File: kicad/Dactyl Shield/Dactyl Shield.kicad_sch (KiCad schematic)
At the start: 10 parts

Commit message: feat: unchecked in changes, likely to LED
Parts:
- TP101, TP102, TP103, TP104: Config (none) -> DNF; Role (none) -> Split

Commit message: doc(sck): better notes on split wire use
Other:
- note added: "The keyboard uses left and right mirrored PCB halves of mostly the same schematic. The schematic differences (below) are for use of the hardware TX/RX for the two wire split. See the shared sub sheet for other details and descriptions."
- note removed: "The keyboard uses left and right mirrored PCB halves of mostly the same schematic. The schematic differences are to use the hardware TX/RX for two wire split. See the shared sub sheet for details and descriptions."
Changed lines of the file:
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@@
 	(title_block
 		(title "Hillside Dactyl Shield")
-		(date "2024-06-04")
+		(date "2025-01-14")
 		(rev "0.1.0-alpha.2")
 		(comment 1 "  Headers: MCU, key matrix and display")
@@
 	(polyline
 		(pts
-			(xy 36.83 171.45) (xy 36.83 203.2)
+			(xy 36.83 172.085) (xy 36.83 203.835)
 		)
 		(stroke
@@
 	(polyline
 		(pts
-			(xy 90.17 57.15) (xy 158.75 57.15)
+			(xy 102.87 50.165) (xy 171.45 50.165)
 		)
 		(stroke
@@
 	(polyline
 		(pts
-			(xy 158.75 67.31) (xy 90.17 67.31)
-		)
-		(stroke
-			(width 0)
-			(type default)
-		)
-	)
-	(polyline
-		(pts
-			(xy 90.17 57.15) (xy 90.17 67.31)
+			(xy 171.45 60.325) (xy 102.87 60.325)
+		)
+		(stroke
+			(width 0)
+			(type default)
+		)
+	)
+	(polyline
+		(pts
+			(xy 102.87 50.165) (xy 102.87 60.325)
 		)
 		(stroke
@@
 	(polyline
 		(pts
-			(xy 158.75 57.15) (xy 158.75 67.31)
+			(xy 171.45 50.165) (xy 171.45 60.325)
 		)
 		(stroke
@@
 	(polyline
 		(pts
-			(xy 158.75 171.45) (xy 36.83 171.45)
-		)
-		(stroke
-			(width 0)
-			(type dash)
-		)
-	)
-	(text_box "Hack to avoid isolated fill warnings\non the paneling side rails."
+			(xy 158.75 172.085) (xy 36.83 172.085)
+		)
+		(stroke
+			(width 0)
+			(type dash)
+		)
+	)
+	(text_box "Hack to avoid warnins about\nisolated fills on the panel side rails."
 		(exclude_from_sim no)
 		(at 107.95 181.61 0)
-		(size 36.83 6.35)
+		(size 38.735 6.35)
 		(stroke
 			(width -0.0001)
@@
 		)
 	)
-	(text_box "USB-C cable use:\n- We aren't sending USB protocal over the split USB-C cable.\n- Our split USB resistors ask for no power, but we accept 5v power in case some accidental computer host isn't doing what it should."
-		(exclude_from_sim no)
-		(at 162.56 141.605 0)
-		(size 48.26 17.78)
+	(text_box "Split USB-C cable use:\n\n- We don't send USB protocal over the split USB-C cable.\n- Yet we follow the protocal in having our split USB resistors ask for no power, and we accept 5v power in case some accidental computer host isn't doing what it should."
+		(exclude_from_sim no)
+		(at 43.815 139.065 0)
+		(size 63.5 13.97)
 		(stroke
 			(width 0)
@@
 		)
 	)
-	(text_box "Caveat:\nI'm not an electrical engineer. This is my best cut at the right approach after much reading plus creating a few boards that seem to work fine. I had EE classes within my CS degrees, but this is outside of that."
-		(exclude_from_sim no)
-		(at 194.945 45.72 0)
+	(text_box "Caveat:\nI'm not an electrical engineer. This is my best cut at the right approach after much reading plus creating a few boards that seem to work fine. I had EE classes in my CS degrees, but this is outside of that."
+		(exclude_from_sim no)
+		(at 194.945 48.895 0)
 		(size 61.595 24.13)
 		(stroke
@@
 		)
 	)
-	(text_box "The wired split can be:\n\n- One wire, though mainly right to left:\n  D+:   Left RX <-> Right TX\n\n- Two wire: \n  D+:   Left RX <-- Right TX \n  D-:   Left TX --> Right RX"
-		(exclude_from_sim no)
-		(at 111.76 139.7 0)
-		(size 45.72 20.955)
+	(text_box "With a wireless split: The UART RX and TX pins can be used for other things.\nSuch as a fifth row or the additional signal line to the Vic connector.\nThough they are wired differently on each board half.\n\nWith a one-wire split: The left RX and right TX pins carry the split, \nand the other can be used for something else.\n\nWith a two-wire split: Both UART RX and TX are used for the split."
+		(exclude_from_sim no)
+		(at 162.56 139.065 0)
+		(size 78.74 18.415)
 		(stroke
 			(width 0)
@@
 		)
 	)
+	(text_box "The wired split can be:\n\n- One wire, though mainly right to left:\n  D+:   Left RX <-> Right TX\n\n- Two wire: \n  D+:   Left RX <-- Right TX \n  D-:   Left TX --> Right RX\n\nBased on firmware needs."
+		(exclude_from_sim no)
+		(at 111.76 139.065 0)
+		(size 45.72 21.59)
+		(stroke
+			(width 0)
+			(type dash)
+		)
+		(fill
+			(type none)
+		)
+		(effects
+			(font
+				(size 1.27 1.27)
+			)
+			(justify left top)
+		)
+	)
 	(text_box "Split\nUSB-C\ncable"
 		(exclude_from_sim no)
@@
 	(text "${TITLE}"
 		(exclude_from_sim no)
-		(at 91.44 64.77 0)
+		(at 104.14 57.785 0)
 		(effects
 			(font
@@
 		)
 	)
-	(text "The keyboard uses left and right mirrored  \nPCB halves of mostly the same schematic.\n\nThe schematic differences are to use the hardware TX/RX\nfor two wire split.\n\nSee the shared sub sheet for details and descriptions."
-		(exclude_from_sim no)
-		(at 90.678 96.266 0)
+	(text "The keyboard uses left and right mirrored  \nPCB halves of mostly the same schematic.\n\nThe schematic differences (below) are for use of the \nhardware TX/RX for the two wire split.\n\nSee the shared sub sheet for other details and descriptions."
+		(exclude_from_sim no)
+		(at 90.678 95.631 0)
 		(effects
 			(font
@@
 	(label "rail_LL"
 		(at 102.87 198.12 0)
-		(fields_autoplaced yes)
 		(effects
 			(font
@@
 	(label "rail_UL"
 		(at 102.87 191.77 0)
-		(fields_autoplaced yes)
 		(effects
 			(font
@@
 	(label "rail_UR"
 		(at 132.08 191.77 0)
-		(fields_autoplaced yes)
 		(effects
 			(font
@@
 	(label "rail_LR"
 		(at 132.08 198.12 0)
-		(fields_autoplaced yes)
-		(effects
-			(font
+		(effects
+			(font

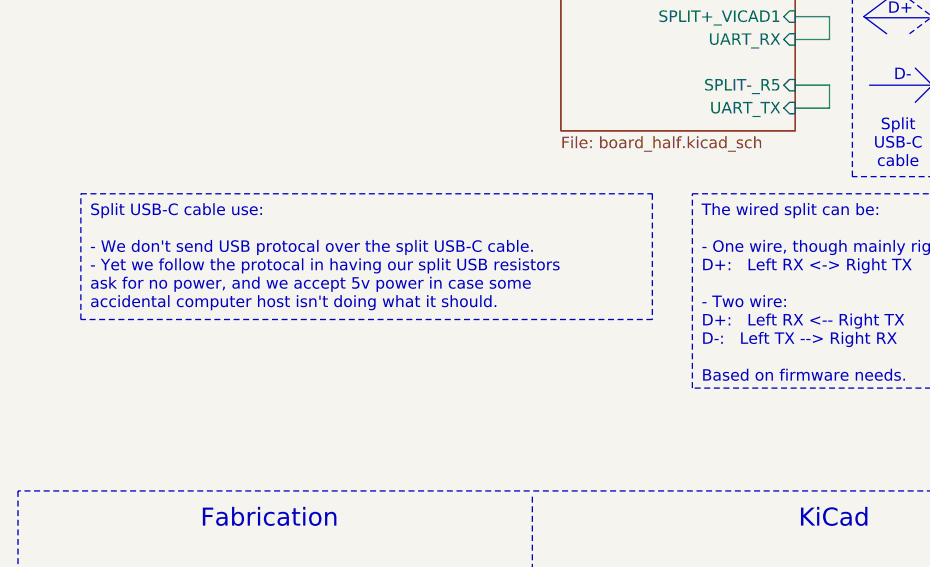
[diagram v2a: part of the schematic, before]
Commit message: refactor: cleanup schematic; external -> foot
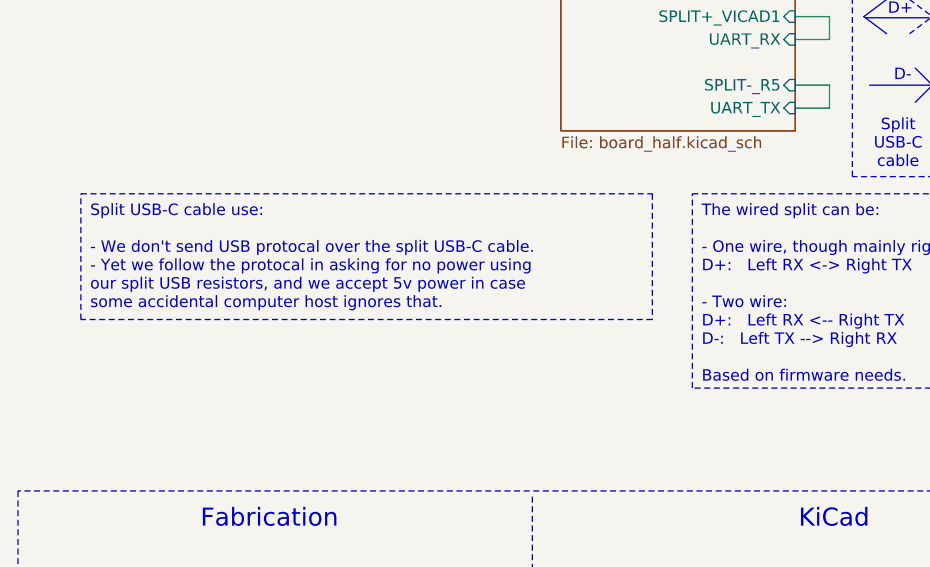
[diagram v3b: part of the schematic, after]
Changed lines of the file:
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@@
 		)
 	)
-	(text_box "Split USB-C cable use:\n\n- We don't send USB protocal over the split USB-C cable.\n- Yet we follow the protocal in having our split USB resistors ask for no power, and we accept 5v power in case some accidental computer host isn't doing what it should."
+	(text_box "Split USB-C cable use:\n\n- We don't send USB protocal over the split USB-C cable.\n- Yet we follow the protocal in asking for no power using our split USB resistors, and we accept 5v power in case some accidental computer host ignores that."
 		(exclude_from_sim no)
 		(at 43.815 139.065 0)

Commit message: feat: use open solder jumpers to LEDs
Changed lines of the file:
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@@
 (kicad_sch
-	(version 20231120)
+	(version 20250114)
 	(generator "eeschema")
-	(generator_version "8.0")
+	(generator_version "9.0")
 	(paper "USLetter")
 	(title_block
@@
 		(comment 4 "Shield for Dactyl split keyboards ")
 	)
+	(text "D-"
+		(exclude_from_sim no)
+		(at 135.128 125.984 0)
+		(effects
+			(font
+				(size 1.27 1.27)
+			)
+		)
+	)
+	(text "5v"
+		(exclude_from_sim no)
+		(at 133.985 111.125 0)
+		(effects
+			(font
+				(size 1.27 1.27)
+			)
+		)
+	)
+	(text "KiCad"
+		(exclude_from_sim no)
+		(at 127.508 175.26 0)
+		(effects
+			(font
+				(size 2 2)
+			)
+		)
+	)
+	(text "Fabrication"
+		(exclude_from_sim no)
+		(at 64.77 175.26 0)
+		(effects
+			(font
+				(size 2 2)
+			)
+		)
+	)
+	(text "${TITLE}"
+		(exclude_from_sim no)
+		(at 104.14 57.785 0)
+		(effects
+			(font
+				(size 4 4)
+			)
+			(justify left bottom)
+		)
+	)
+	(text "D+"
+		(exclude_from_sim no)
+		(at 134.874 118.618 0)
+		(effects
+			(font
+				(size 1.27 1.27)
+			)
+		)
+	)
+	(text "GND"
+		(exclude_from_sim no)
+		(at 133.985 114.935 0)
+		(effects
+			(font
+				(size 1.27 1.27)
+			)
+		)
+	)
+	(text "The keyboard uses left and right mirrored  \nPCB halves of mostly the same schematic.\n\nThe schematic differences (below) are for use of the \nhardware TX/RX for the two wire split.\n\nSee the shared sub sheet for other details and descriptions."
+		(exclude_from_sim no)
+		(at 90.678 95.631 0)
+		(effects
+			(font
+				(size 2.5 2.5)
+			)
+			(justify left bottom)
+		)
+	)
+	(text_box "Hack to avoid warnins about\nisolated fills on the panel side rails."
+		(exclude_from_sim no)
+		(at 107.95 181.61 0)
+		(size 38.735 6.35)
+		(margins 0.9524 0.9524 0.9524 0.9524)
+		(stroke
+			(width -0.0001)
+			(type default)
+		)
+		(fill
+			(type none)
+		)
+		(effects
+			(font
+				(size 1.27 1.27)
+			)
+			(justify left top)
+		)
+	)
+	(text_box "Split USB-C cable use:\n\n- We don't send USB protocal over the split USB-C cable.\n- Yet we follow the protocal in asking for no power using our split USB resistors, and we accept 5v power in case some accidental computer host ignores that."
+		(exclude_from_sim no)
+		(at 43.815 139.065 0)
+		(size 63.5 13.97)
+		(margins 0.9525 0.9525 0.9525 0.9525)
+		(stroke
+			(width 0)
+			(type dash)
+		)
+		(fill
+			(type none)
+		)
+		(effects
+			(font
+				(size 1.27 1.27)
+			)
+			(justify left top)
+		)
+	)
+	(text_box "Caveat:\nI'm not an electrical engineer. This is my best cut at the right approach after much reading plus creating a few boards that seem to work fine. I had EE classes in my CS degrees, but this is outside of that."
+		(exclude_from_sim no)
+		(at 194.945 48.895 0)
+		(size 61.595 24.13)
+		(margins 1.5 1.5 1.5 1.5)
+		(stroke
+			(width 0)
+			(type dash)
+		)
+		(fill
+			(type none)
+		)
+		(effects
+			(font
+				(size 2 2)
+			)
+			(justify left top)
+		)
+	)
+	(text_box "With a wireless split: The UART RX and TX pins can be used for other things.\nSuch as a fifth row or the additional signal line to the Vic connector.\nThough they are wired differently on each board half.\n\nWith a one-wire split: The left RX and right TX pins carry the split, \nand the other can be used for something else.\n\nWith a two-wire split: Both UART RX and TX are used for the split."
+		(exclude_from_sim no)
+		(at 162.56 139.065 0)
+		(size 78.74 18.415)
+		(margins 0.9525 0.9525 0.9525 0.9525)
+		(stroke
+			(width 0)
+			(type dash)
+		)
+		(fill
+			(type none)
+		)
+		(effects
+			(font
+				(size 1.27 1.27)
+			)
+			(justify left top)
+		)
+	)
+	(text_box "The wired split can be:\n\n- One wire, though mainly right to left:\n  D+:   Left RX <-> Right TX\n\n- Two wire: \n  D+:   Left RX <-- Right TX \n  D-:   Left TX --> Right RX\n\nBased on firmware needs."
+		(exclude_from_sim no)
+		(at 111.76 139.065 0)
+		(size 45.72 21.59)
+		(margins 0.9525 0.9525 0.9525 0.9525)
+		(stroke
+			(width 0)
+			(type dash)
+		)
+		(fill
+			(type none)
+		)
+		(effects
+			(font
+				(size 1.27 1.27)
+			)
+			(justify left top)
+		)
+	)
+	(text_box "Split\nUSB-C\ncable"
+		(exclude_from_sim no)
+		(at 129.54 109.22 0)
+		(size 10.16 27.94)
+		(margins 0.9525 0.9525 0.9525 0.9525)
+		(stroke
+			(width 0)
+			(type dash)
+		)
+		(fill
+			(type none)
+		)
+		(effects
+			(font
+				(size 1.27 1.27)
+			)
+			(justify bottom)
+		)
+	)
 	(junction
 		(at 110.49 191.77)
@@
 			(width 0)
 			(type dash)
-		)
-	)
-	(text_box "Hack to avoid warnins about\nisolated fills on the panel side rails."
-		(exclude_from_sim no)
-		(at 107.95 181.61 0)
-		(size 38.735 6.35)
-		(stroke
-			(width -0.0001)
-			(type default)
-		)
-		(fill
-			(type none)
-		)
-		(effects
-			(font
-				(size 1.27 1.27)
-			)
-			(justify left top)
-		)
-	)
-	(text_box "Split USB-C cable use:\n\n- We don't send USB protocal over the split USB-C cable.\n- Yet we follow the protocal in asking for no power using our split USB resistors, and we accept 5v power in case some accidental computer host ignores that."
-		(exclude_from_sim no)
-		(at 43.815 139.065 0)
-		(size 63.5 13.97)
-		(stroke
-			(width 0)
-			(type dash)
-		)
-		(fill
-			(type none)
-		)
-		(effects
-			(font
-				(size 1.27 1.27)
-			)
-			(justify left top)
-		)
-	)
-	(text_box "Caveat:\nI'm not an electrical engineer. This is my best cut at the right approach after much reading plus creating a few boards that seem to work fine. I had EE classes in my CS degrees, but this is outside of that."
-		(exclude_from_sim no)
-		(at 194.945 48.895 0)
-		(size 61.595 24.13)
-		(stroke
-			(width 0)
-			(type dash)
-		)
-		(fill
-			(type none)
-		)
-		(effects
-			(font
-				(size 2 2)
-			)
-			(justify left top)
-		)
-	)
-	(text_box "With a wireless split: The UART RX and TX pins can be used for other things.\nSuch as a fifth row or the additional signal line to the Vic connector.\nThough they are wired differently on each board half.\n\nWith a one-wire split: The left RX and right TX pins carry the split, \nand the other can be used for something else.\n\nWith a two-wire split: Both UART RX and TX are used for the split."
-		(exclude_from_sim no)
-		(at 162.56 139.065 0)
-		(size 78.74 18.415)
-		(stroke
-			(width 0)
-			(type dash)
-		)
-		(fill
-			(type none)
-		)
-		(effects
-			(font
-				(size 1.27 1.27)
-			)
-			(justify left top)
-		)
-	)
-	(text_box "The wired split can be:\n\n- One wire, though mainly right to left:\n  D+:   Left RX <-> Right TX\n\n- Two wire: \n  D+:   Left RX <-- Right TX \n  D-:   Left TX --> Right RX\n\nBased on firmware needs."
-		(exclude_from_sim no)
-		(at 111.76 139.065 0)
-		(size 45.72 21.59)
-		(stroke
-			(width 0)
-			(type dash)
-		)
-		(fill
-			(type none)
-		)
-		(effects
-			(font
-				(size 1.27 1.27)
-			)
-			(justify left top)
-		)
-	)
-	(text_box "Split\nUSB-C\ncable"
-		(exclude_from_sim no)
-		(at 129.54 109.22 0)
-		(size 10.16 27.94)
-		(stroke
-			(width 0)
-			(type dash)
-		)
-		(fill
-			(type none)
-		)
-		(effects
-			(font
-				(size 1.27 1.27)
-			)
-			(justify bottom)
-		)
-	)
-	(text "D-"
-		(exclude_from_sim no)
-		(at 135.128 125.984 0)
-		(effects
-			(font
-				(size 1.27 1.27)
-			)
-		)
-	)
-	(text "5v"
-		(exclude_from_sim no)
-		(at 133.985 111.125 0)
-		(effects
-			(font
-				(size 1.27 1.27)
-			)
-		)
-	)
-	(text "KiCad"
-		(exclude_from_sim no)
-		(at 127.508 175.26 0)
-		(effects
-			(font
-				(size 2 2)
-			)
-		)
-	)
-	(text "Fabrication"
-		(exclude_from_sim no)
-		(at 64.77 175.26 0)
-		(effects
-			(font
-				(size 2 2)
-			)
-		)
-	)
-	(text "${TITLE}"
-		(exclude_from_sim no)
-		(at 104.14 57.785 0)
-		(effects
-			(font
-				(size 4 4)
-			)
-			(justify left bottom)
-		)
-	)
-	(text "D+"
-		(exclude_from_sim no)
-		(at 134.874 118.618 0)
-		(effects
-			(font
-				(size 1.27 1.27)
-			)
-		)
-	)
-	(text "GND"
-		(exclude_from_sim no)
-		(at 133.985 114.935 0)
-		(effects
-			(font
-				(size 1.27 1.27)
-			)
-		)
-	)
-	(text "The keyboard uses left and right mirrored  \nPCB halves of mostly the same schematic.\n\nThe schematic differences (below) are for use of the \nhardware TX/RX for the two wire split.\n\nSee the shared sub sheet for other details and descriptions."
-		(exclude_from_sim no)
-		(at 90.678 95.631 0)
-		(effects
-			(font
-				(size 2.5 2.5)
-			)
-			(justify left bottom)
 		)
 	)
@@
 		(at 49.53 190.5 0)
 		(unit 1)
-		(exclude_from_sim yes)
+		(exclude_from_sim no)
 		(in_bom no)
 		(on_board yes)
@@
 		(at 73.66 190.5 0)
 		(unit 1)
-		(exclude_from_sim yes)
+		(exclude_from_sim no)
 		(in_bom no)
 		(on_board yes)
@@
 		(at 73.66 196.85 0)
 		(unit 1)
-		(exclude_from_sim yes)
+		(exclude_from_sim no)
 		(in_bom no)
 		(on_board yes)
@@
 		(at 49.53 184.15 0)
 		(unit 1)
-		(exclude_from_sim yes)
+		(exclude_from_sim no)
 		(in_bom no)
 		(on_board yes)
@@
 		(at 73.66 184.15 0)
 		(unit 1)
-		(exclude_from_sim yes)
+		(exclude_from_sim no)
 		(in_bom no)
 		(on_board yes)
@@
 		(at 49.53 196.85 0)
 		(unit 1)
-		(exclude_from_sim yes)
+		(exclude_from_sim no)
 		(in_bom no)
 		(on_board yes)
@@
 		(at 97.155 109.22)
 		(size 26.035 22.86)
+		(exclude_from_sim no)
+		(in_bom yes)
+		(on_board yes)
+		(dnp no)
 		(fields_autoplaced yes)
 		(stroke
@@
 		(at 146.05 109.22)
 		(size 26.035 22.86)
+		(exclude_from_sim no)
+		(in_bom yes)
+		(on_board yes)
+		(dnp no)
 		(fields_autoplaced yes)
 		(stroke
@@
 		)
 	)
+	(embedded_fonts no)
 )
